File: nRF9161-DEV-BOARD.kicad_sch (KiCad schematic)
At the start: 0 parts

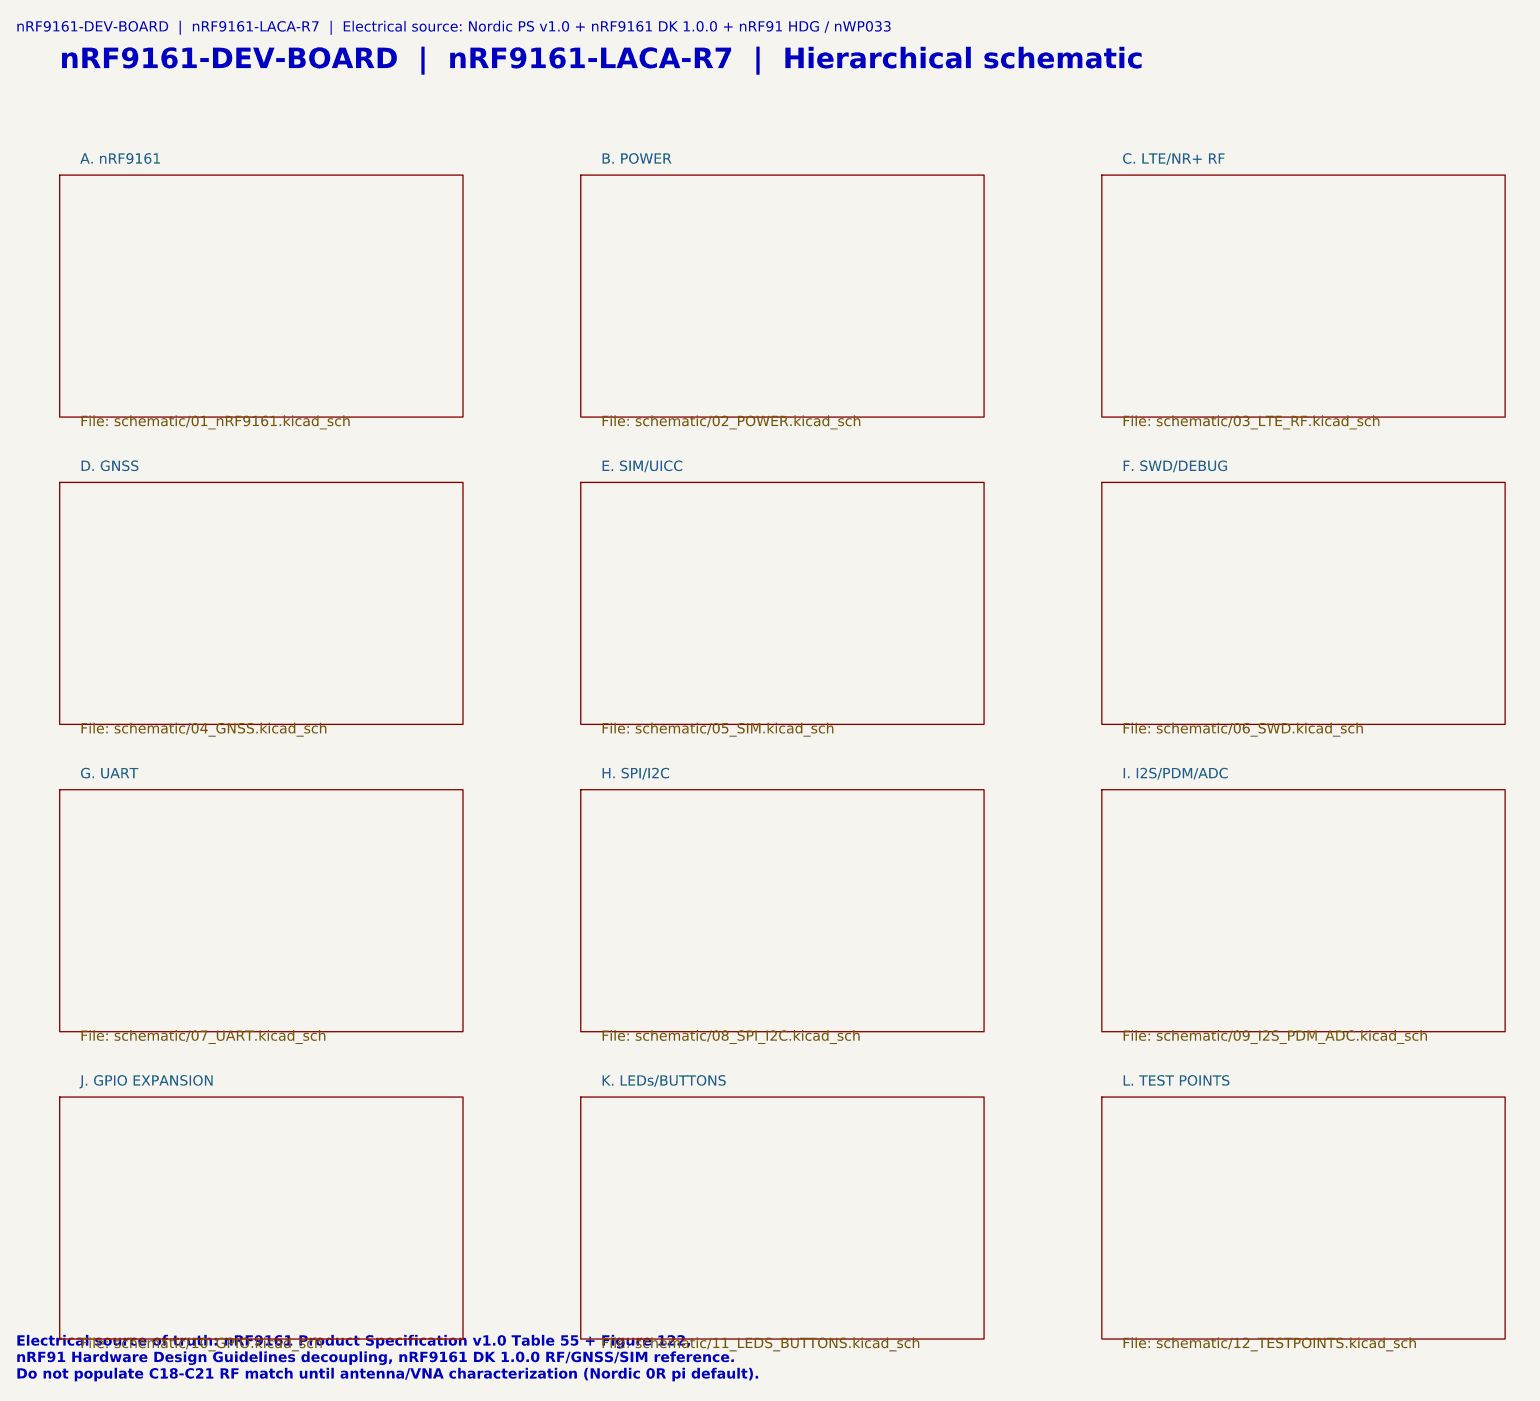
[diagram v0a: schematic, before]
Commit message: v2: simplify to UART modem module (J20 host header, LXC translators); remove J1, J3, J6, J9-J18, optional parts
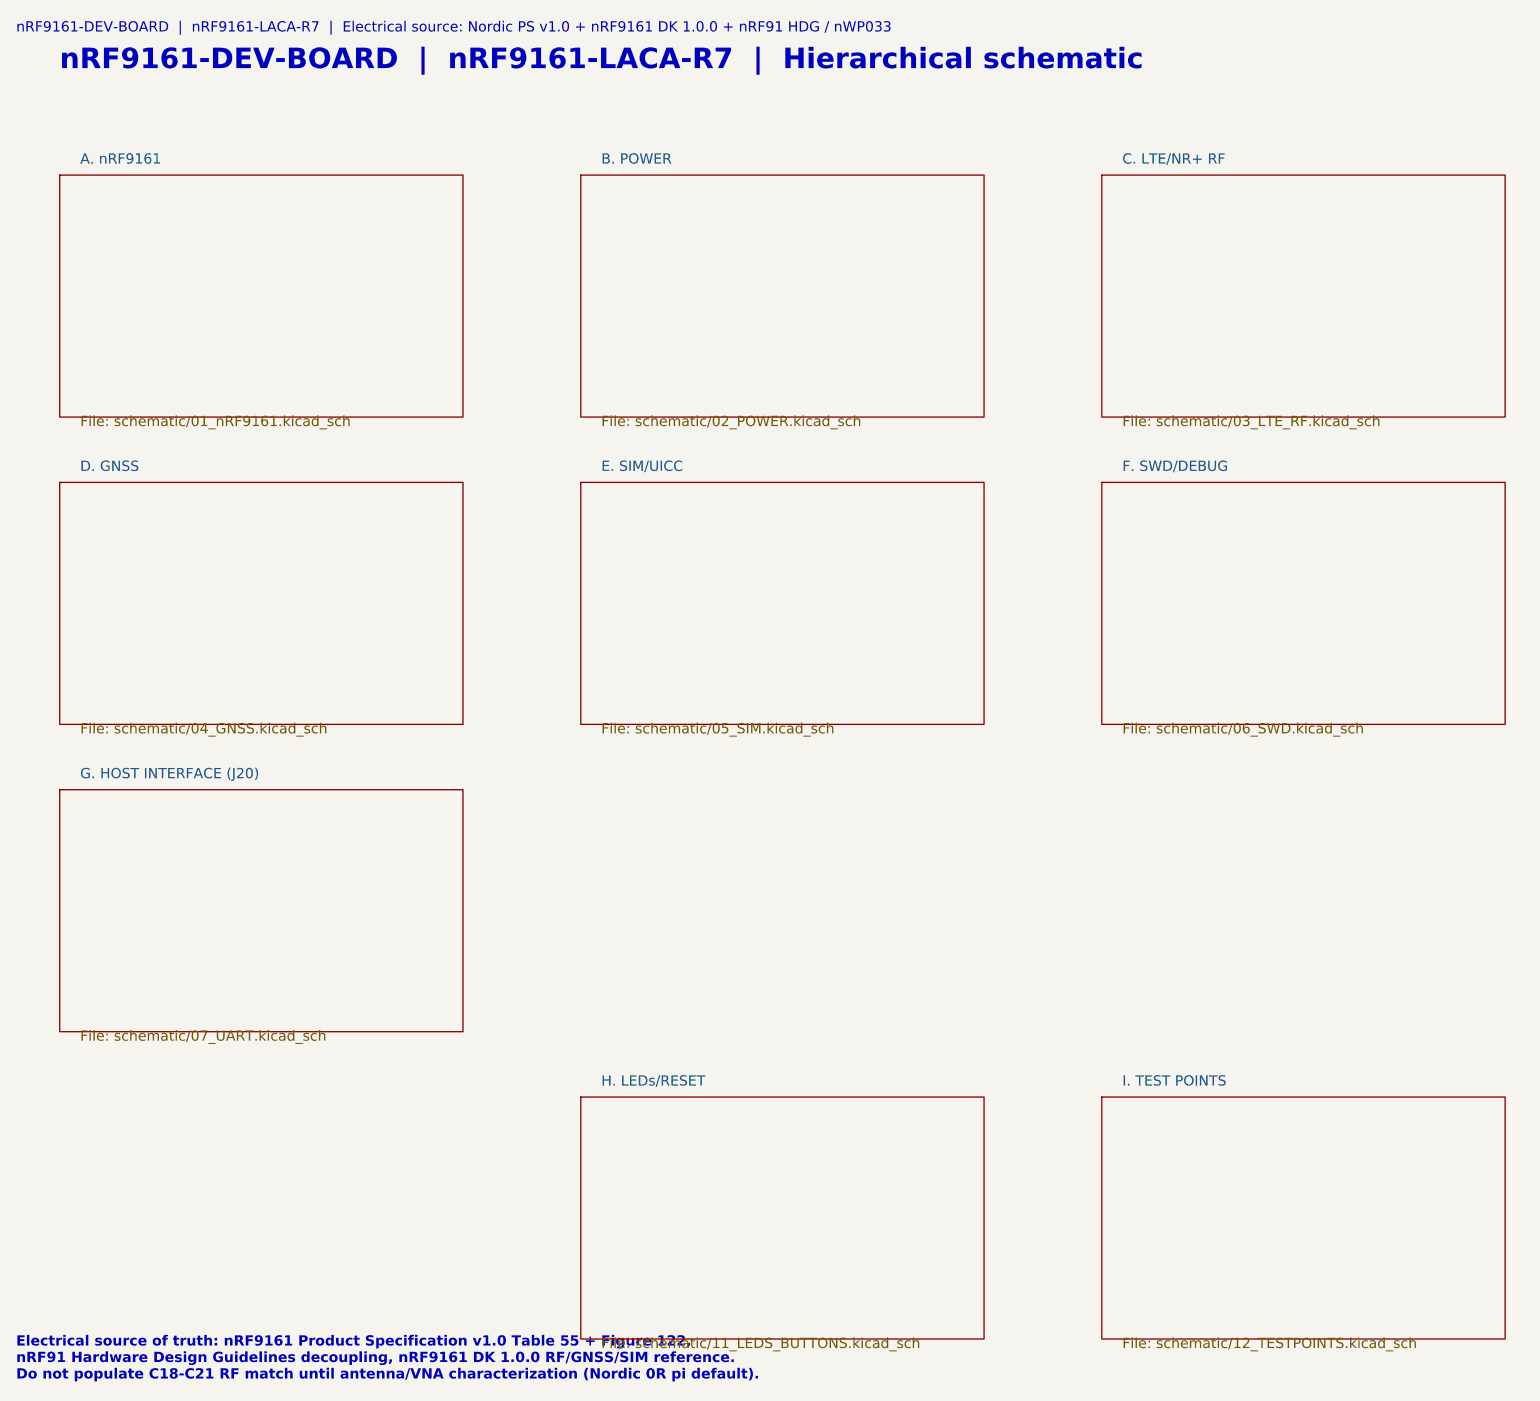
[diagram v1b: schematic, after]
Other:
- sheet G. UART renamed G. HOST INTERFACE (J20)
- sheet K. LEDs/BUTTONS renamed H. LEDs/RESET
- sheet L. TEST POINTS renamed I. TEST POINTS
- removed sheet H. SPI/I2C
- removed sheet I. I2S/PDM/ADC
- removed sheet J. GPIO EXPANSION
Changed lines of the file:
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@@
     (stroke (width 0.0006) (type default))
     (fill (color 0 0 0 0.0000))
-    (property "Sheet name" "G. UART" (at 27.94 100.33 0)
+    (property "Sheet name" "G. HOST INTERFACE (J20)" (at 27.94 100.33 0)
       (effects (font (size 1.27 1.27)) (justify left bottom))
     )
@@
     )
   )
-  (sheet (at 90.0 101.6) (size 50.0 30.0) (fields_autoplaced yes)
-    (stroke (width 0.0006) (type default))
-    (fill (color 0 0 0 0.0000))
-    (property "Sheet name" "H. SPI/I2C" (at 92.54 100.33 0)
-      (effects (font (size 1.27 1.27)) (justify left bottom))
-    )
-    (property "Sheet file" "schematic/08_SPI_I2C.kicad_sch" (at 92.54 132.87 0)
-      (effects (font (size 1.27 1.27)) (justify left bottom))
-    )
-  )
-  (sheet (at 154.6 101.6) (size 50.0 30.0) (fields_autoplaced yes)
-    (stroke (width 0.0006) (type default))
-    (fill (color 0 0 0 0.0000))
-    (property "Sheet name" "I. I2S/PDM/ADC" (at 157.14 100.33 0)
-      (effects (font (size 1.27 1.27)) (justify left bottom))
-    )
-    (property "Sheet file" "schematic/09_I2S_PDM_ADC.kicad_sch" (at 157.14 132.87 0)
-      (effects (font (size 1.27 1.27)) (justify left bottom))
-    )
-  )
-  (sheet (at 25.4 139.7) (size 50.0 30.0) (fields_autoplaced yes)
-    (stroke (width 0.0006) (type default))
-    (fill (color 0 0 0 0.0000))
-    (property "Sheet name" "J. GPIO EXPANSION" (at 27.94 138.43 0)
-      (effects (font (size 1.27 1.27)) (justify left bottom))
-    )
-    (property "Sheet file" "schematic/10_GPIO.kicad_sch" (at 27.94 170.97 0)
-      (effects (font (size 1.27 1.27)) (justify left bottom))
-    )
-  )
   (sheet (at 90.0 139.7) (size 50.0 30.0) (fields_autoplaced yes)
     (stroke (width 0.0006) (type default))
     (fill (color 0 0 0 0.0000))
-    (property "Sheet name" "K. LEDs/BUTTONS" (at 92.54 138.43 0)
+    (property "Sheet name" "H. LEDs/RESET" (at 92.54 138.43 0)
       (effects (font (size 1.27 1.27)) (justify left bottom))
     )
@@
     (stroke (width 0.0006) (type default))
     (fill (color 0 0 0 0.0000))
-    (property "Sheet name" "L. TEST POINTS" (at 157.14 138.43 0)
+    (property "Sheet name" "I. TEST POINTS" (at 157.14 138.43 0)
       (effects (font (size 1.27 1.27)) (justify left bottom))
     )
@@
       (path "/e1caf6a7-e2a0-4ff1-8424-4d92c0348b6b/771cec44-91bf-49a5-8340-cd824d7c5092" (page "7"))
       (path "/e1caf6a7-e2a0-4ff1-8424-4d92c0348b6b/d42bc010-aba6-416b-b465-dd1a45e916de" (page "8"))
-      (path "/e1caf6a7-e2a0-4ff1-8424-4d92c0348b6b/08644c31-ed6f-48a3-a952-fcb31a88cbf8" (page "9"))
-      (path "/e1caf6a7-e2a0-4ff1-8424-4d92c0348b6b/af29c727-61dc-4c84-9136-62d2e9719b29" (page "10"))
-      (path "/e1caf6a7-e2a0-4ff1-8424-4d92c0348b6b/626201db-df36-41b2-8dca-cf7cb365ca58" (page "11"))
-      (path "/e1caf6a7-e2a0-4ff1-8424-4d92c0348b6b/875f8df2-b476-452a-ae42-3ddb22327da8" (page "12"))
-      (path "/e1caf6a7-e2a0-4ff1-8424-4d92c0348b6b/6094c42a-44ea-4b9f-82fd-f46adfb0569c" (page "13"))
+      (path "/e1caf6a7-e2a0-4ff1-8424-4d92c0348b6b/875f8df2-b476-452a-ae42-3ddb22327da8" (page "9"))
+      (path "/e1caf6a7-e2a0-4ff1-8424-4d92c0348b6b/6094c42a-44ea-4b9f-82fd-f46adfb0569c" (page "10"))
   )
 )
